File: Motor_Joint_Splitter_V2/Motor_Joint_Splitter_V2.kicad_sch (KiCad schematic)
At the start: 17 parts, among them J1 Conn_01x08, J2 54602-908LF, J4 26605030, J7 Conn_01x05, U1 74ACT244MTCX

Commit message: Still a work in progress. The molex connectors used by the USM motors are surface mounts, looking for compatible through-hole headers instead.
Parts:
- added C1, C2: 1uF, PCM_JLCPCB:C_0402, symbol PCM_JLCPCB-Capacitors:0402,1uF
- added H1, H2: MountingHole_Pad, MountingHole:MountingHole_3.2mm_M3_DIN965_Pad_TopBottom, symbol Mechanical:MountingHole_Pad
- J1: footprint Connector_JST:JST_XH_B8B-XH-A_1x08_P2.50mm_Vertical -> Connector_JST:JST_ZH_B8B-ZR_1x08_P1.50mm_Vertical
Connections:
- net +5V: now also C1.1, C2.2
- net GND: now also U1.11 (I7), U1.13 (I6), U1.7 (O6), U1.9 (O7), C1.2, C2.1, H1.1, H2.1
- no-connect marks 4 -> 0
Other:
- moved on the sheet: R13, R14, R15, R16, R17, R19

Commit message: Updated the PCB design and library for added parts.
Need to find pre-crimped wires for making the female-to-female 5-pin connector. Outside of that, everything else that's already picked should work fine.
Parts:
- removed C2: 1uF, PCM_JLCPCB:C_0402, symbol PCM_JLCPCB-Capacitors:0402,1uF
- removed J2: 54602-908LF, ethernet_connector:AMPHENOL_54602-908LF, symbol ethernet_connector:54602-908LF
- removed J7: Conn_01x05, Connector_JST:JST_EH_B5B-EH-A_1x05_P2.50mm_Vertical, symbol Connector_Generic:Conn_01x05
- added C3, C4: 1uF, PCM_JLCPCB:C_0402, symbol PCM_JLCPCB-Capacitors:0402,1uF
- added J2: 26605030, CONN_SDA-41792_M450_03_MOL, symbol splitter_parts:26605030
- added J3: motor_conn_1x8_P2.54_705550007, CONN_705550000-SD_08_MOL, symbol splitter_library:motor_conn_1x8_P2.54_705550007
- added J5: Conn_01x05, Connector_JST:JST_EH_B5B-EH-A_1x05_P2.50mm_Vertical, symbol Connector_Generic:Conn_01x05
- added J6: molex_conn_1x5_P2.54_705530004, splitter_parts:CONN_70553-XXXX_05_MOL, symbol splitter_parts:molex_conn_1x5_P2.54_705530004
- added J7: ethernet_54602-908LF, splitter_parts:AMPHENOL_54602-908LF, symbol splitter_parts:ethernet_54602-908LF
- added J8: molex_conn_2x4_P2.54_702470851, CONN_7024708xx_MOL, symbol splitter_parts:molex_conn_2x4_P2.54_702470851
- added J9: molex_conn_2x3_P2.54_901303106, splitter_parts:CONN_SDA-90130_RA_06_MOL, symbol splitter_parts:molex_conn_2x3_P2.54_901303106
- added U2: 74ACT244MTCX, splitter_parts:line_driver_SOP65P640X120-20N, symbol splitter_parts:line_driver_74ACT244MTCX
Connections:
- net +5V: now also C3.1, C4.2, J3.5, J5.4 (Pin_4), J6.2, J7.1, J8.5, J9.2, U2.20 (VCC)
- net C_A: now also J3.3, J8.3, U2.6 (I2)
- net C_A_Out: now also U2.14 (O2)
- net C_A_Out_2: now also J7.2
- net C_B: now also J3.2, J8.2, U2.8 (I3)
- net C_B_Out: now also U2.12 (O3)
- net C_B_Out_2: now also J7.3
- net C_I: now also J3.1, J8.1, U2.2 (I0)
- net C_I_Out: now also U2.18 (O0)
- net C_I_Out_2: now also J7.4
- net Cos: now also J2.2, J3.6, J8.6
- net GND: now also C3.2, C4.1, J2.3, J3.4, J3.7, J5.1 (Pin_1), J6.5, J7.8, J8.4, J8.7, J9.5, J9.6, U2.1 (~OE1), U2.10 (GND), U2.11 (I7), U2.13 (I6), U2.19 (~OE2), U2.7 (O6), U2.9 (O7)
- net SEA_A: now also J5.3 (Pin_3), J6.4, J9.4, U2.15 (I5)
- net SEA_A_Out: now also U2.5 (O5)
- net SEA_A_Out_2: now also J7.6
- net SEA_B: now also J5.5 (Pin_5), J6.1, J9.1, U2.17 (I4)
- net SEA_B_Out: now also U2.3 (O4)
- net SEA_B_Out_2: now also J7.7
- net SEA_I: now also J5.2 (Pin_2), J6.3, J9.3, U2.4 (I1)
- net SEA_I_Out: now also U2.16 (O1)
- net SEA_I_Out_2: now also J7.5
- net Sin: now also J2.1, J3.8, J8.8
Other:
- note added: "Old - For Reference"
- note added: "Power Cables"
- note removed: "Control Cables"
- moved on the sheet: C1, J1, J4, U1

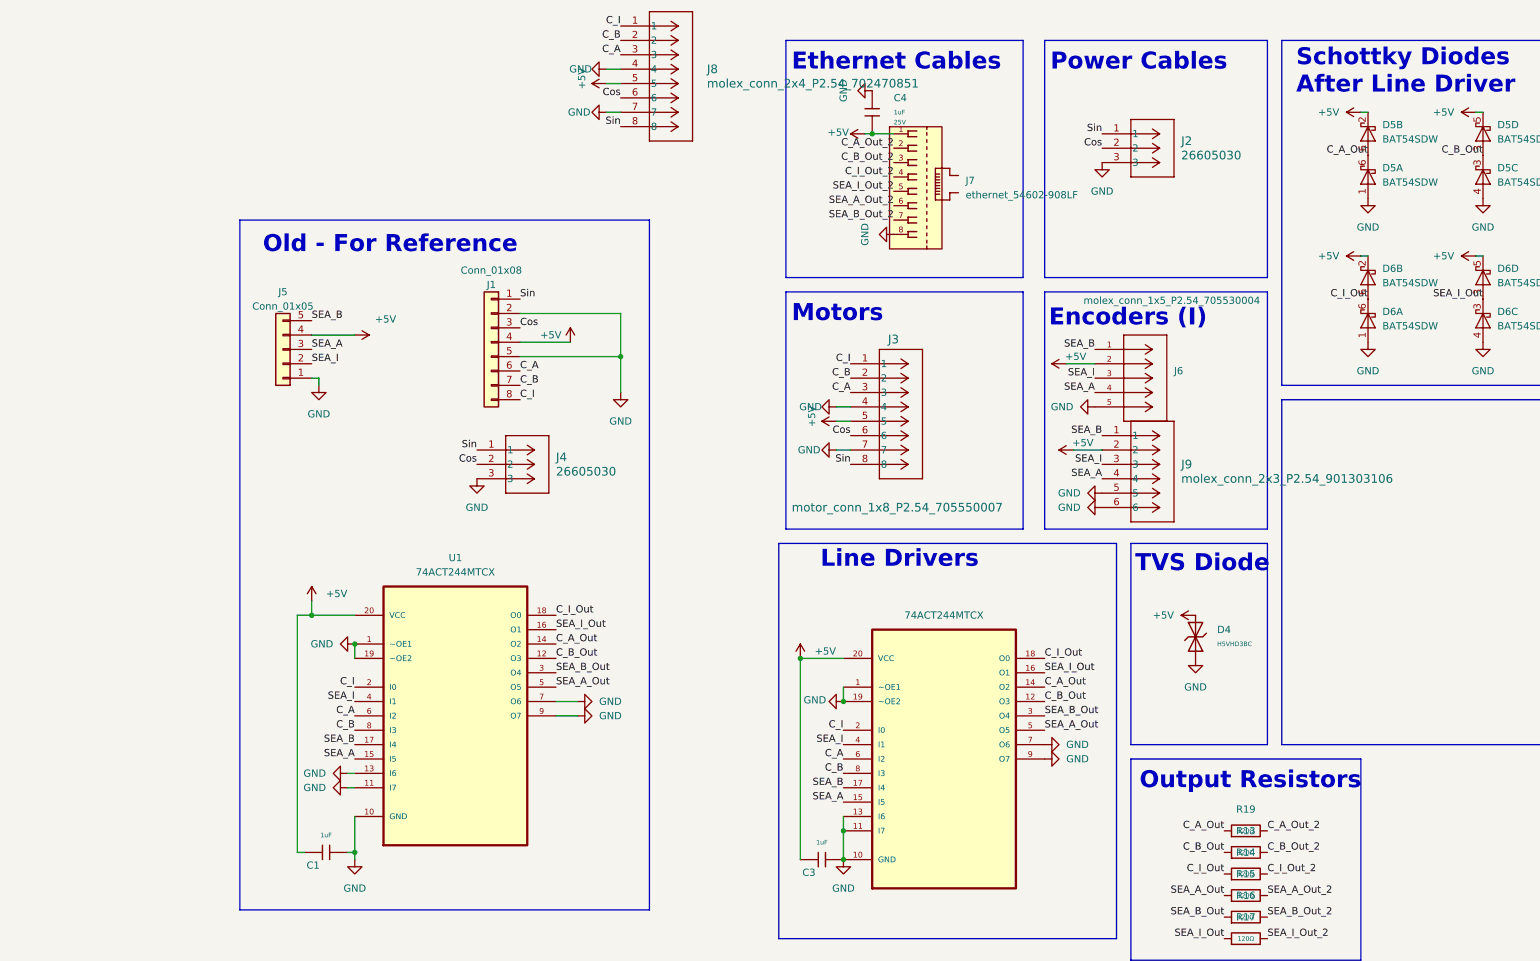
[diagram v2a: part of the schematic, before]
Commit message: Updated the headers, should all be good now. Need to double check the routing to make sure it's not going to be an issue.
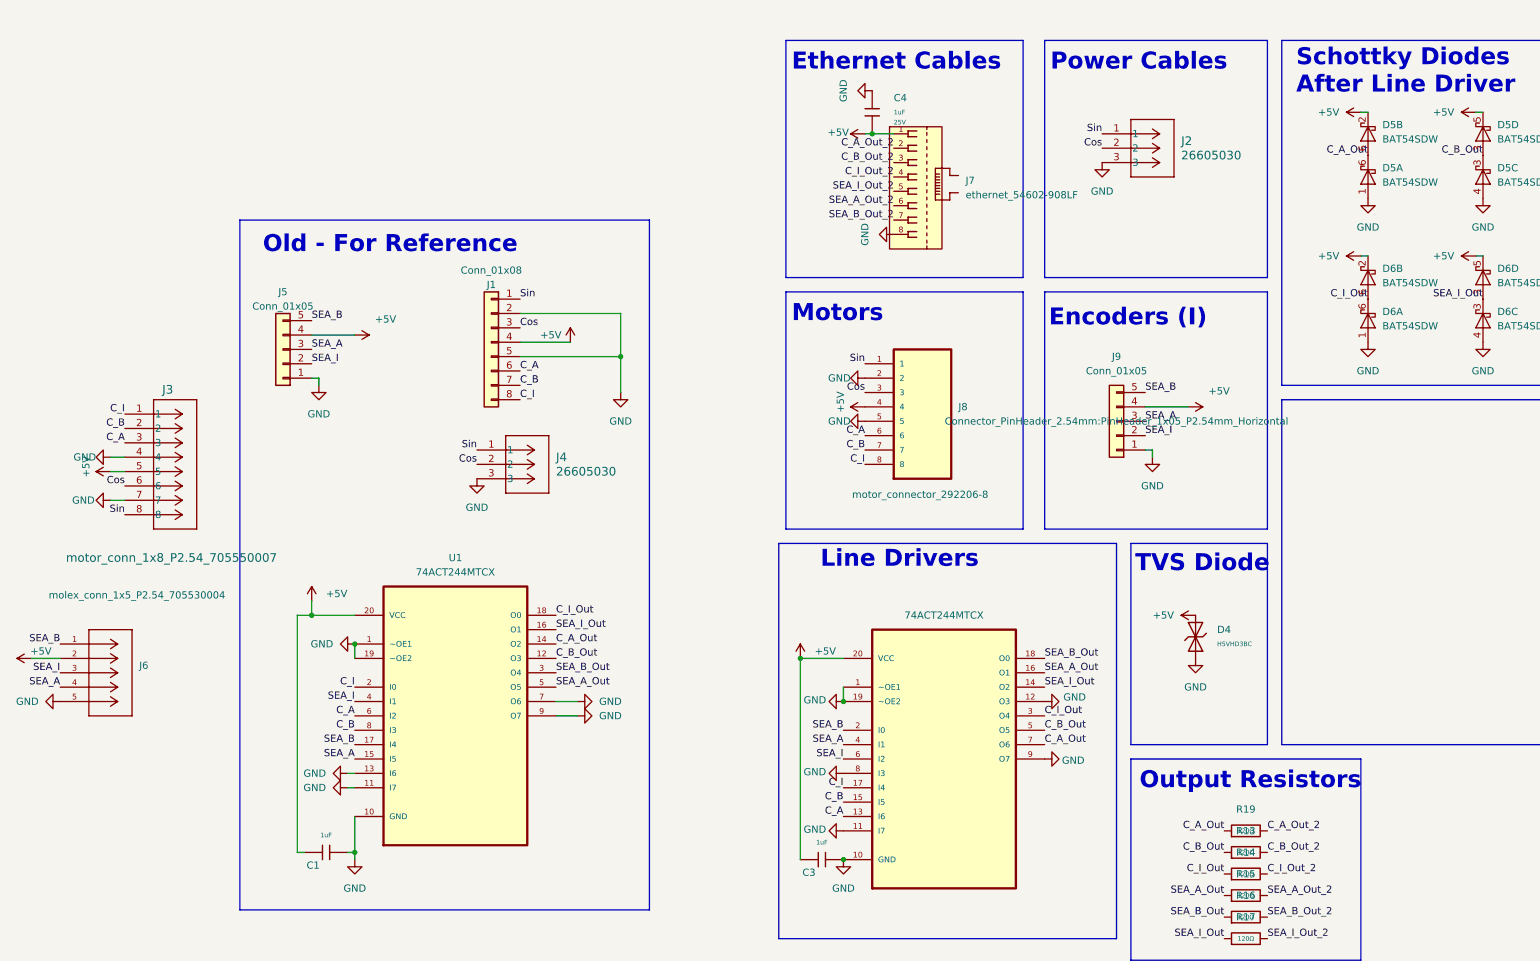
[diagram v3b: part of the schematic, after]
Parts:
- removed J8: molex_conn_2x4_P2.54_702470851, CONN_7024708xx_MOL, symbol splitter_parts:molex_conn_2x4_P2.54_702470851
- removed J9: molex_conn_2x3_P2.54_901303106, splitter_parts:CONN_SDA-90130_RA_06_MOL, symbol splitter_parts:molex_conn_2x3_P2.54_901303106
- added J8: motor_connector_292206-8, splitter_parts:TE_292206-8, symbol splitter_parts:motor_connector_292206-8
- added J9: Conn_01x05, Connector_PinHeader_2.54mm:PinHeader_1x05_P2.54mm_Horizontal, symbol Connector_Generic:Conn_01x05
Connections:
- net +5V: now also J8.4, J9.4 (Pin_4)
- net C_A: now also U2.13 (I6), J8.6; no longer U2.6 (I2)
- net C_A_Out: now also U2.7 (O6); no longer U2.14 (O2)
- net C_B: now also U2.15 (I5), J8.7; no longer U2.8 (I3)
- net C_B_Out: now also U2.5 (O5); no longer U2.12 (O3)
- net C_I: now also U2.17 (I4), J8.8; no longer U2.2 (I0)
- net C_I_Out: now also U2.3 (O4); no longer U2.18 (O0)
- net Cos: now also J8.3
- net GND: now also U2.12 (O3), U2.8 (I3), J8.2, J8.5, J9.1 (Pin_1); no longer U2.13 (I6), U2.7 (O6)
- net SEA_A: now also U2.4 (I1), J9.3 (Pin_3); no longer U2.15 (I5)
- net SEA_A_Out: now also U2.16 (O1); no longer U2.5 (O5)
- net SEA_B: now also U2.2 (I0), J9.5 (Pin_5); no longer U2.17 (I4)
- net SEA_B_Out: now also U2.18 (O0); no longer U2.3 (O4)
- net SEA_I: now also U2.6 (I2), J9.2 (Pin_2); no longer U2.4 (I1)
- net SEA_I_Out: now also U2.14 (O2); no longer U2.16 (O1)
- net Sin: now also J8.1
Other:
- moved on the sheet: J3, J6

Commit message: Board seems mostly complete. Need to verify parts list and gerber files are fine next.
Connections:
- net C_A_Out: now also D7.3 (A), D7.3 (K); no longer D5.6 (A), D5.6 (K)
- net C_I_Out: now also D5.6 (A), D5.6 (K); no longer D6.6 (A), D6.6 (K)
- net SEA_A_Out: now also D6.6 (A), D6.6 (K); no longer D7.6 (A), D7.6 (K)
- net SEA_B_Out: now also D6.3 (A), D6.3 (K); no longer D7.3 (A), D7.3 (K)
- net SEA_I_Out: now also D7.6 (A), D7.6 (K); no longer D6.3 (A), D6.3 (K)
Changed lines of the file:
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@@
+		)
+	)
+	(label "C_I_Out"
+		(at 118.11 35.56 180)
+		(effects
+			(font
+				(size 1.27 1.27)
+			)
+			(justify right bottom)
 		)
 	)
@@
 		)
 	)
+	(label "C_A_Out"
+		(at 180.34 35.56 180)
+		(effects
+			(font
+				(size 1.27 1.27)
+			)
+			(justify right bottom)
+		)
+	)
 	(label "SEA_A_Out"
 		(at -25.4 129.54 0)
@@
 		)
 	)
-	(label "SEA_A_Out"
-		(at 160.02 35.56 180)
-		(effects
-			(font
-				(size 1.27 1.27)
-			)
-			(justify right bottom)
-		)
-	)
 	(label "Cos"
 		(at -101.6 93.98 180)
@@
 		)
 	)
+	(label "SEA_B_Out"
+		(at 138.43 60.96 180)
+		(effects
+			(font
+				(size 1.27 1.27)
+			)
+			(justify right bottom)
+		)
+	)
 	(label "C_I_Out_2"
 		(at 100.33 162.56 0)
@@
 		)
 	)
-	(label "C_I_Out"
-		(at 118.11 60.96 180)
-		(effects
-			(font
-				(size 1.27 1.27)
-			)
-			(justify right bottom)
-		)
-	)
 	(label "C_A_Out_2"
 		(at 34.29 34.29 180)
@@
 		)
 	)
+	(label "SEA_I_Out"
+		(at 160.02 35.56 180)
+		(effects
+			(font
+				(size 1.27 1.27)
+			)
+			(justify right bottom)
+		)
+	)
 	(label "SEA_B_Out_2"
 		(at 34.29 46.99 180)
@@
 		)
 	)
-	(label "SEA_B_Out"
-		(at 180.34 35.56 180)
+	(label "SEA_A_Out"
+		(at 118.11 60.96 180)
 		(effects
 			(font
@@
 		)
 	)
-	(label "C_A_Out"
-		(at 118.11 35.56 180)
-		(effects
-			(font
-				(size 1.27 1.27)
-			)
-			(justify right bottom)
-		)
-	)
 	(label "SEA_A_Out"
 		(at 60.96 127 0)
@@
 		)
 	)
-	(label "SEA_I_Out"
-		(at 138.43 60.96 180)
+	(label "SEA_A"
+		(at 25.4 139.7 180)
 		(effects
 			(font
@@
 		(effects
 			(font
-				(size 1.27 1.27)
-			)
-			(justify right bottom)
-		)
-	)
-	(label "SEA_A"
-		(at 25.4 139.7 180)
-		(effects
-			(font
